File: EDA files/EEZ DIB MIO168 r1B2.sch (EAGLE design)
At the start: 296 parts, among them IC1 M24C32-WMN6P, IC10 DAC7760IPWPR, IC11 DAC7760IPWPR, IC12 OPA376AIDBVR, IC13 DAC7563TDGSR, IC14 OPA2196IDR, IC15 BTS3408G, IC16 BTS3408G, IC17 BTS3408G, IC18 BTS3408G, IC19 74HC126PW,118, IC2 Si8641BB-B-IS1, IC20 TL431B, IC21 DG468DV-T1-E3, IC22 DG468DV-T1-E3, IC23 DG468DV-T1-E3, IC24 DG468DV-T1-E3, IC25 DG468DV-T1-E3, IC26 DG468DV-T1-E3, IC27 DG468DV-T1-E3, IC28 DG468DV-T1-E3, IC29 DG468DV-T1-E3, IC3 Si8641BB-B-IS1, IC30 DG468DV-T1-E3, IC31 DG468DV-T1-E3, IC32 DG468DV-T1-E3, IC33 DG468DV-T1-E3, IC34 DG468DV-T1-E3, IC35 OPA376AIDBVR, IC36 ADS8674IDBT, IC4 L78L12, IC5 LP2985-50DBVR, IC6 LP2985-33DBVR, IC7 L79L12, IC8 STM32F446ZCT6, IC9 OPA2196IDR, J1 4907, J2 N.C., Q1 2N7002PS,115, Q10 BSS169, Q11 BSS169, Q12 BSS169, Q13 BSS169, Q2 2N7002PS,115, Q3 2N7002PS,115, Q4 2N7002PS,115, Q5 2N7002PS,115, Q6 BSS169, Q7 BSS169, Q8 BSS169, Q9 BSS169, X1 77317-104-28LF, X2 SSW-106-02-S-S, X3 691327310016, X4 691327310016, Y1 25MHz

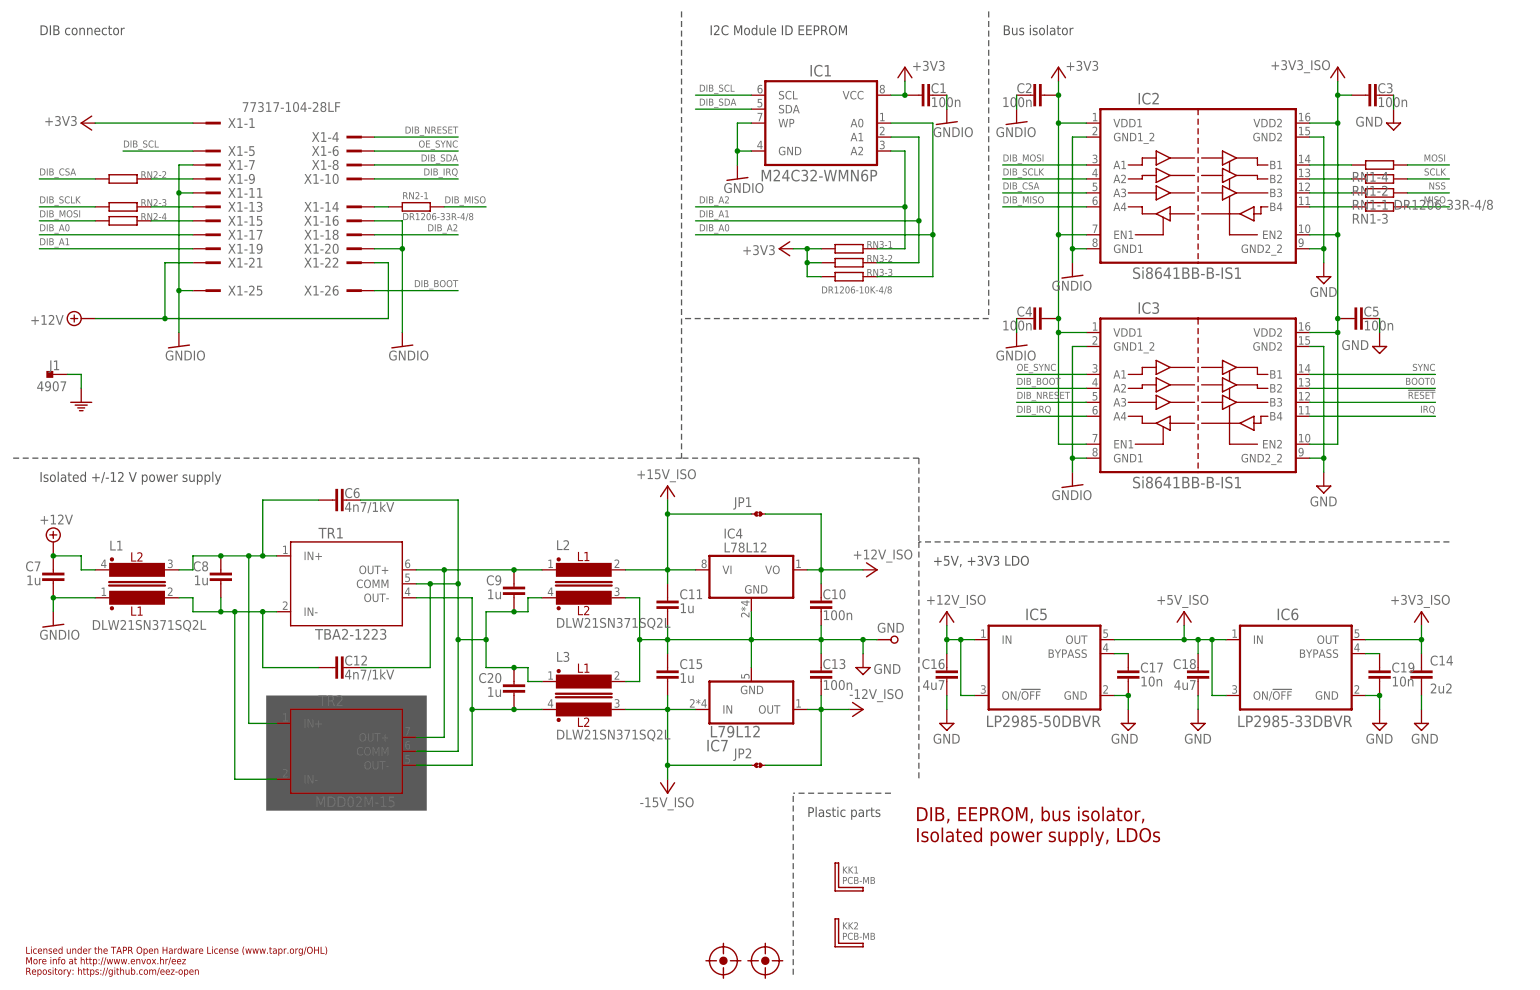
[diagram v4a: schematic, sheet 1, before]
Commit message: IRQ selection jumper
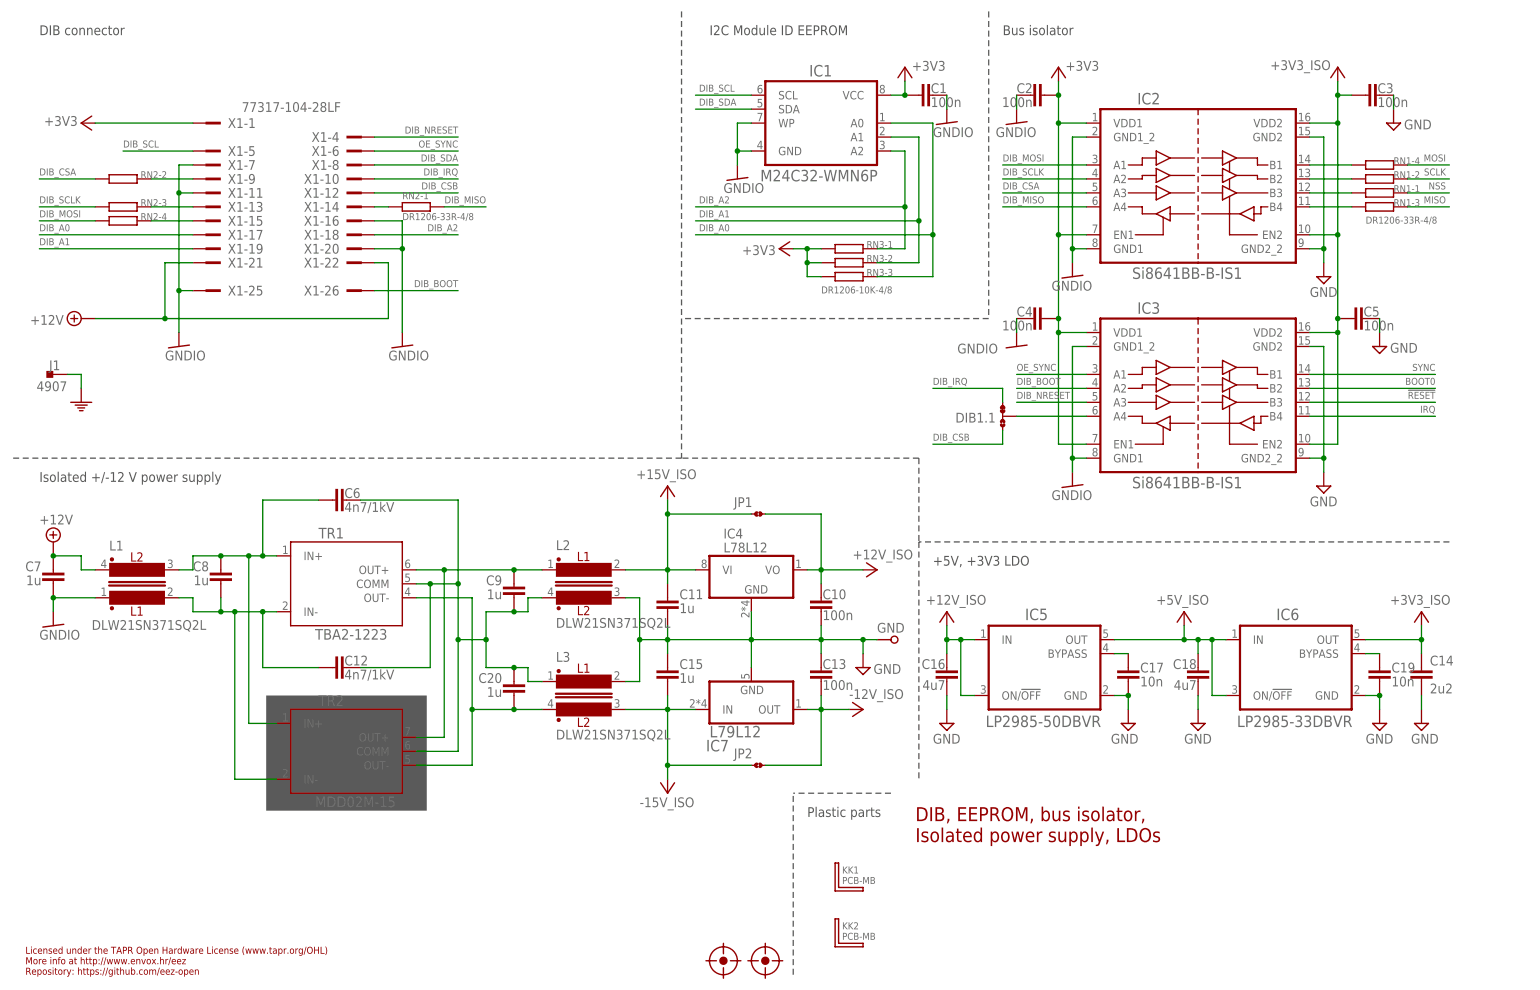
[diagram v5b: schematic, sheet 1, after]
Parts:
- added DIB1.1: JP3-CUT-0805-ROTATED, EEZ_Lib1:JP3-CUT-0805-ROTATED
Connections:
- new net DIB_CSB: DIB1.1.NO, X1-12.1
- new net N$11: DIB1.1.COM, IC3.A4
- net DIB_IRQ: now also DIB1.1.NC; no longer IC3.A4
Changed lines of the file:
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@@
 <setting verticaltext="up"/>
 </settings>
-<grid distance="0.1" unitdist="inch" unit="inch" style="lines" multiple="1" display="no" altdistance="0.01" altunitdist="inch" altunit="inch"/>
+<grid distance="0.025" unitdist="inch" unit="inch" style="lines" multiple="4" display="no" altdistance="0.01" altunitdist="inch" altunit="inch"/>
 <layers>
 <layer number="1" name="Top" color="4" fill="1" visible="no" active="no"/>
@@
 <layer number="111" name="111" color="7" fill="1" visible="no" active="no"/>
 <layer number="112" name="tSilk" color="7" fill="1" visible="no" active="no"/>
+<layer number="113" name="ReferenceLS" color="7" fill="1" visible="yes" active="yes"/>
 <layer number="114" name="EEZ" color="12" fill="1" visible="yes" active="yes"/>
 <layer number="116" name="Patch_BOT" color="7" fill="1" visible="no" active="no"/>
@@
 <part name="GND" library="EEZ_Lib1" deviceset="PCB_TEST_TAB" device="SHIELD"/>
 <part name="SUPPLY27" library="supply2" deviceset="GND" device=""/>
+<part name="DIB1.1" library="EEZ_Lib1" deviceset="JP3-CUT" device="-0805-ROTATED"/>
 </parts>
 <sheets>
@@
 </instance>
 <instance part="SUPPLY57" gate="GND" x="251.46" y="157.48" smashed="yes">
-<attribute name="VALUE" x="249.555" y="156.845" size="1.778" layer="96" rot="MR0"/>
+<attribute name="VALUE" x="253.365" y="158.115" size="1.778" layer="96" rot="MR180"/>
 </instance>
 <instance part="GND13" gate="G$1" x="182.88" y="157.48" smashed="yes">
@@
 </instance>
 <instance part="GND9" gate="G$1" x="182.88" y="116.84" smashed="yes">
-<attribute name="VALUE" x="179.07" y="114.3" size="1.778" layer="96"/>
+<attribute name="VALUE" x="172.085" y="115.57" size="1.778" layer="96"/>
 </instance>
 <instance part="C5" gate="G$1" x="246.38" y="121.92" smashed="yes" rot="MR90">
@@
 </instance>
 <instance part="SUPPLY56" gate="GND" x="248.92" y="116.84" smashed="yes">
-<attribute name="VALUE" x="247.015" y="116.205" size="1.778" layer="96" rot="MR0"/>
+<attribute name="VALUE" x="250.825" y="117.475" size="1.778" layer="96" rot="MR180"/>
 </instance>
 <instance part="GND10" gate="G$1" x="193.04" y="91.44" smashed="yes">
@@
 </instance>
 <instance part="RN1" gate="-4" x="248.92" y="149.86" smashed="yes">
-<attribute name="NAME" x="243.84" y="146.812" size="1.778" layer="95"/>
+<attribute name="NAME" x="251.46" y="149.987" size="1.27" layer="95"/>
 </instance>
 <instance part="RN1" gate="-1" x="248.92" y="144.78" smashed="yes">
-<attribute name="VALUE" x="251.46" y="141.732" size="1.778" layer="96"/>
-<attribute name="NAME" x="243.84" y="141.732" size="1.778" layer="95"/>
-</instance>
-<instance part="RN1" gate="-3" x="248.92" y="142.24"/>
-<instance part="RN1" gate="-2" x="248.92" y="147.32"/>
+<attribute name="VALUE" x="246.38" y="139.192" size="1.27" layer="96"/>
+<attribute name="NAME" x="251.46" y="144.907" size="1.27" layer="95"/>
+</instance>
+<instance part="RN1" gate="-3" x="248.92" y="142.24" smashed="yes">
+<attribute name="NAME" x="251.46" y="142.367" size="1.27" layer="95"/>
+</instance>
+<instance part="RN1" gate="-2" x="248.92" y="147.32" smashed="yes">
+<attribute name="NAME" x="251.46" y="147.447" size="1.27" layer="95"/>
+</instance>
+<instance part="DIB1.1" gate="G$1" x="180.34" y="104.14" smashed="yes" rot="MR180">
+<attribute name="NAME" x="179.07" y="104.775" size="1.778" layer="95" rot="R180"/>
+</instance>
+<instance part="X1" gate="-12" x="66.04" y="144.78"/>
 </instances>
 <busses>
@@
 </segment>
 <segment>
-<wire x1="182.88" y1="104.14" x2="195.58" y2="104.14" width="0.1524" layer="91"/>
-<label x="182.88" y="104.775" size="1.27" layer="102"/>
-<pinref part="IC3" gate="A" pin="A4"/>
+<label x="167.64" y="109.855" size="1.27" layer="102"/>
+<pinref part="DIB1.1" gate="G$1" pin="NC"/>
+<wire x1="167.64" y1="109.22" x2="180.34" y2="109.22" width="0.1524" layer="91"/>
+<wire x1="180.34" y1="109.22" x2="180.34" y2="106.68" width="0.1524" layer="91"/>
 </segment>
 </net>
@@
 </segment>
 </net>
+<net name="DIB_CSB" class="0">
+<segment>
+<pinref part="DIB1.1" gate="G$1" pin="NO"/>
+<wire x1="180.34" y1="101.6" x2="180.34" y2="99.06" width="0.1524" layer="91"/>
+<wire x1="180.34" y1="99.06" x2="167.64" y2="99.06" width="0.1524" layer="91"/>
+<label x="167.64" y="99.695" size="1.27" layer="102"/>
+</segment>
+<segment>
+<pinref part="X1" gate="-12" pin="1"/>
+<wire x1="66.04" y1="144.78" x2="81.28" y2="144.78" width="0.1524" layer="91"/>
+<label x="81.28" y="145.415" size="1.27" layer="102" rot="MR0"/>
+</segment>
+</net>
+<net name="N$11" class="0">
+<segment>
+<pinref part="DIB1.1" gate="G$1" pin="COM"/>
+<pinref part="IC3" gate="A" pin="A4"/>
+<wire x1="182.88" y1="104.14" x2="195.58" y2="104.14" width="0.1524" layer="91"/>
+</segment>
+</net>
